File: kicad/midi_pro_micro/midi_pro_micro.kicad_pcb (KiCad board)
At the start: 2 copper layers, 160 x 44 mm, 23 parts, among them J1 DIN-5_180degree, J2 DIN-5_180degree, J3 Conn_01x12, J4 Conn_01x16_Pin, J6 Conn_01x04, U1 ProMicro, U2 AT25xxx, U3 6N138

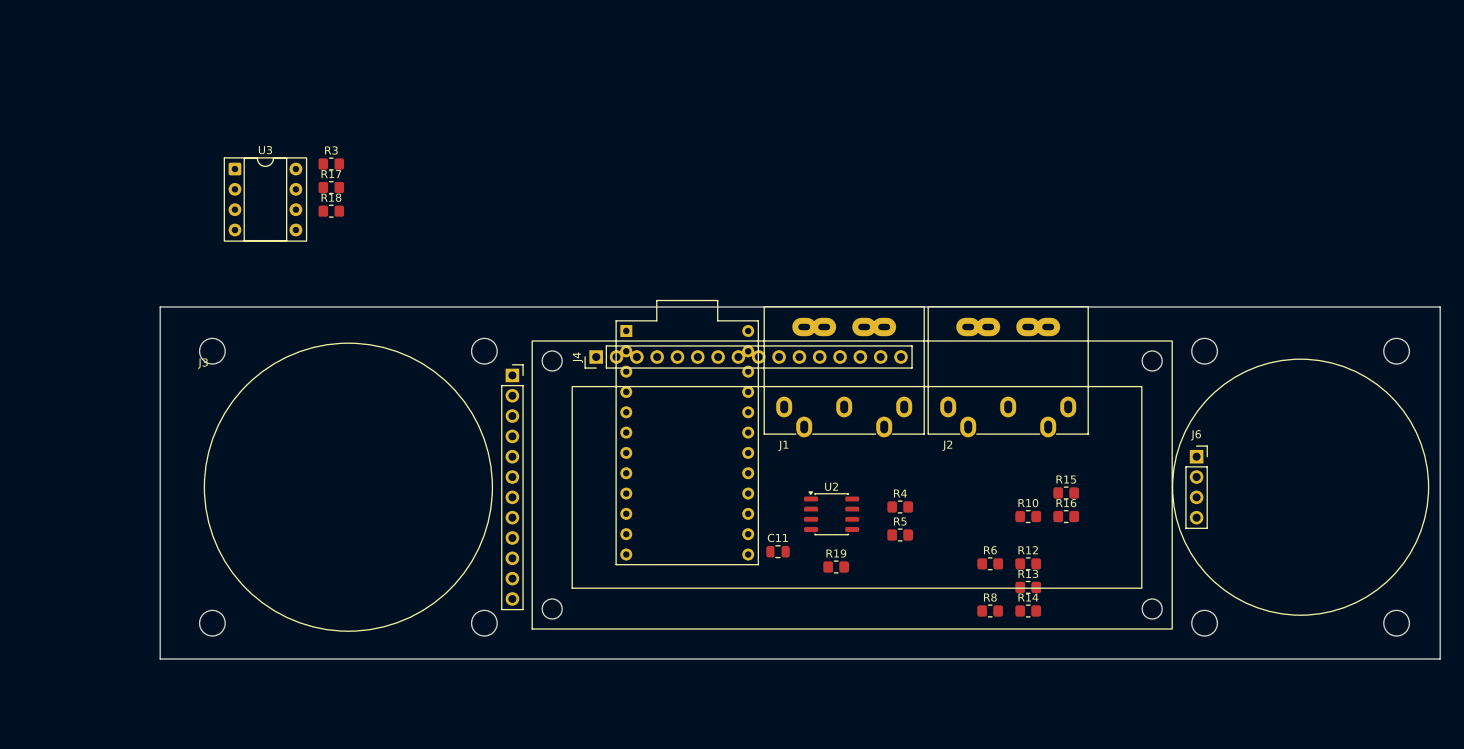
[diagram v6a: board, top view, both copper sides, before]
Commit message: Add case body prototype
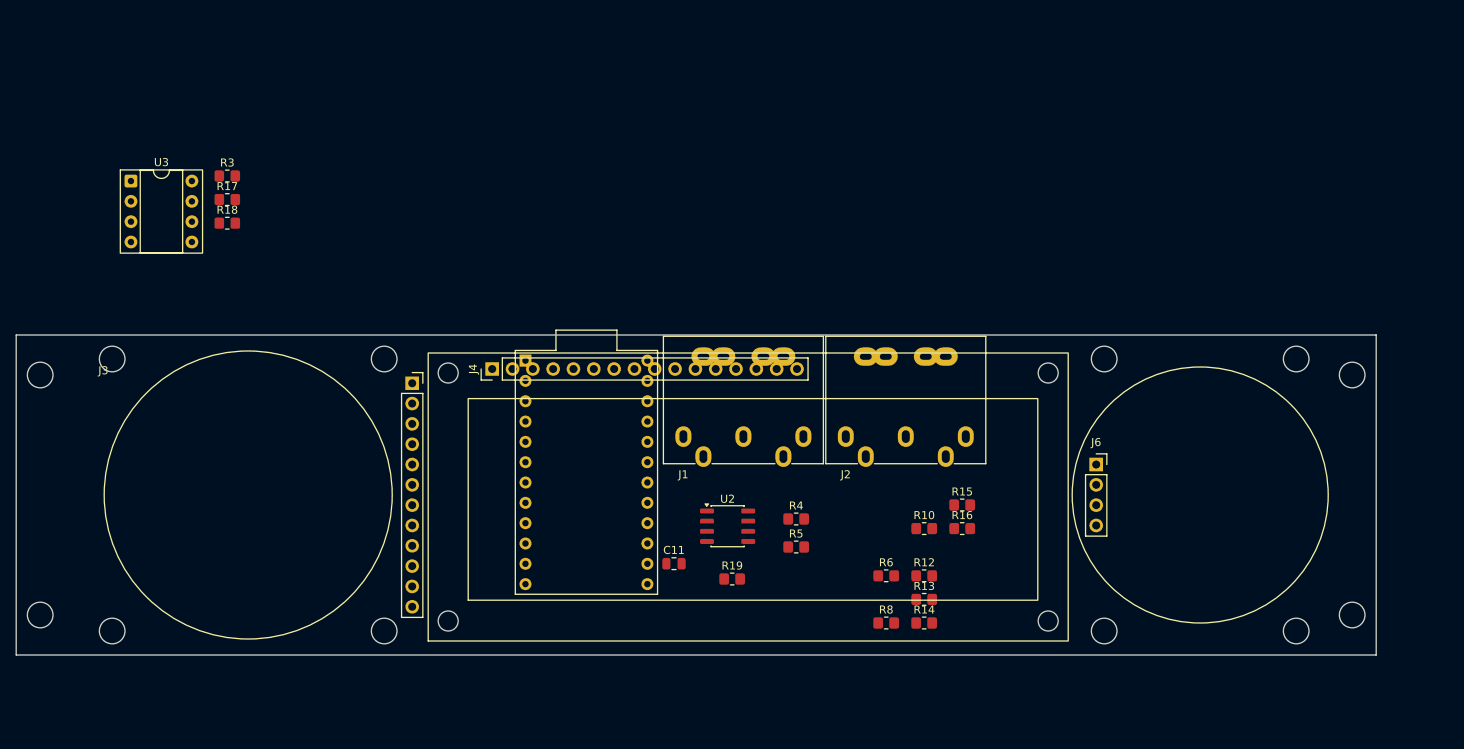
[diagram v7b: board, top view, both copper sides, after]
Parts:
- added H1: MountingHole, MountingHole:MountingHole_3.2mm_M3_DIN965, F.Cu at (68.0, 85.0)
- added H2: MountingHole, MountingHole:MountingHole_3.2mm_M3_DIN965, F.Cu at (68.0, 115.0)
- added H3: MountingHole, MountingHole:MountingHole_3.2mm_M3_DIN965, F.Cu at (232.0, 85.0)
- added H4: MountingHole, MountingHole:MountingHole_3.2mm_M3_DIN965, F.Cu at (232.0, 115.0)
- moved J2 13.3 mm to (168.7, 92.7)
- moved J1 13.1 mm to (148.4, 92.7)
- moved U1 13.1 mm to (136.3, 97.2)
- moved C11 13.1 mm to (147.2, 108.6)
- moved J4 13.1 mm to (124.5, 84.2)
- moved R10 13.1 mm to (178.5, 104.2)
- moved R12 13.1 mm to (178.5, 110.1)
- moved R13 13.1 mm to (178.5, 113.0)
- moved R14 13.1 mm to (178.5, 116.0)
- moved R15 13.1 mm to (183.2, 101.2)
- moved R16 13.1 mm to (183.2, 104.2)
- moved R17 13.1 mm to (91.4, 63.1)
- moved R18 13.1 mm to (91.4, 66.0)
- moved R19 13.1 mm to (154.5, 110.5)
- moved R3 13.1 mm to (91.4, 60.1)
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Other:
- board size 160 x 44 mm -> 170 x 40 mm

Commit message: Basic layout ready
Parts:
- removed J4: Conn_01x16_Pin, Connector_PinHeader_2.54mm:PinHeader_1x16_P2.54mm_Vertical
- added H11: Conn_01x16_Pin, lib:OLED_1602_mechanical, F.Cu at (117.1, 81.7)
- added J5: Conn_01x05, Connector_JST:JST_PH_B5B-PH-K_1x05_P2.00mm_Vertical, F.Cu at (155.2, 115.7)
- added J7: Conn_01x02, Connector_JST:JST_PH_B2B-PH-K_1x02_P2.00mm_Vertical, F.Cu at (126.2, 115.2)
- moved U3 94.3 mm to (164.0, 102.4), turned to -90 degrees
- moved R17 90.8 mm to (169.0, 110.3), turned to 180 degrees
- moved R3 78.2 mm to (159.5, 98.5)
- moved R18 75.0 mm to (151.9, 110.4), turned to 180 degrees
- moved R10 70.9 mm to (107.6, 103.8)
- moved R6 69.7 mm to (107.5, 88.7)
- moved R8 69.1 mm to (107.5, 96.2)
- moved R19 46.9 mm to (107.7, 108.9)
- moved U1 43.8 mm to (180.1, 97.8)
- moved R12 41.7 mm to (137.0, 105.6), turned to -90 degrees
- moved J2 36.2 mm to (132.5, 92.5)
- moved R14 32.8 mm to (206.4, 98.8), turned to 180 degrees
- moved R13 32.7 mm to (145.9, 110.3), turned to -90 degrees
- moved R5 27.6 mm to (135.9, 99.0)
- moved R16 24.5 mm to (206.4, 96.2), turned to 180 degrees
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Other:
- outline, holes or cut-outs redrawn
